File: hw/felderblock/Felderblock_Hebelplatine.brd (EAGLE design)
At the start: 50 x 78 mm, 35 parts, among them IC3 MCP23017SP, X1 I2C-1, X4 I2C-2

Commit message: tweaked layout
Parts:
- moved R25 2.84 mm to (7.62, 41.9)
- moved R27 2.54 mm to (7.62, 38.7)
- moved R16 1.91 mm to (27.9, 38.7)
- moved R20 1.90 mm to (27.9, 34.9)
- moved R28 1.27 mm to (27.9, 25.4)
- moved R22 0.64 mm to (27.9, 74.3)
- turned LED5 to 0 degrees
- turned LED6 to 0 degrees
- turned LED7 to 0 degrees
- turned LED8 to 0 degrees
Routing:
- net FST6_LED: track 34.7 -> 37.3 mm
- net FST8: track 35.6 -> 37.5 mm
- net FST4_LED: track 49.6 -> 51.3 mm
- net N$15: track 5.91 -> 4.60 mm
- net N$12: track 6.88 -> 8.09 mm
- net N$10: track 9.31 -> 10.5 mm
- net FST5: track 55.7 -> 54.6 mm
- net FST7_LED: track 58.2 -> 57.1 mm
- net FST7: track 20.9 -> 21.5 mm
- net FST3_LED: track 29.2 -> 28.6 mm

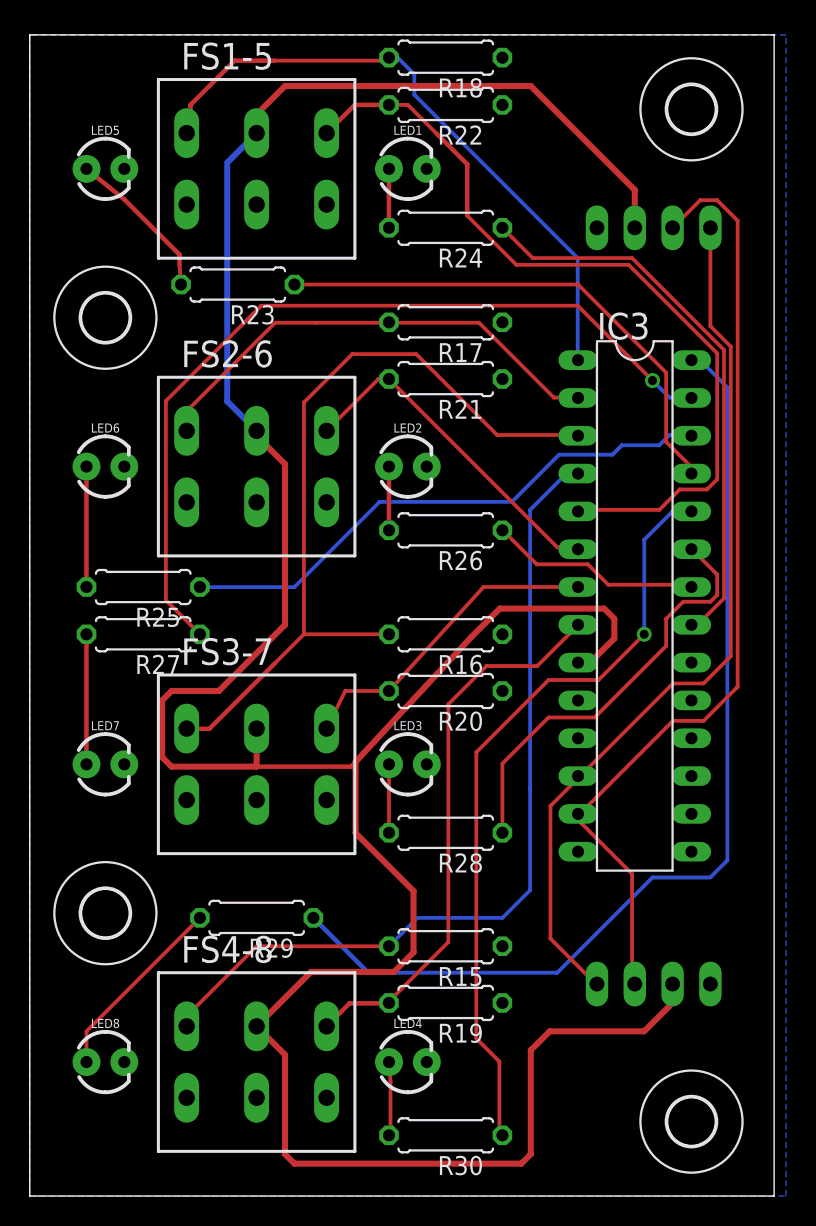
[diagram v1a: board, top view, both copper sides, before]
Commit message: moved I2C connectors
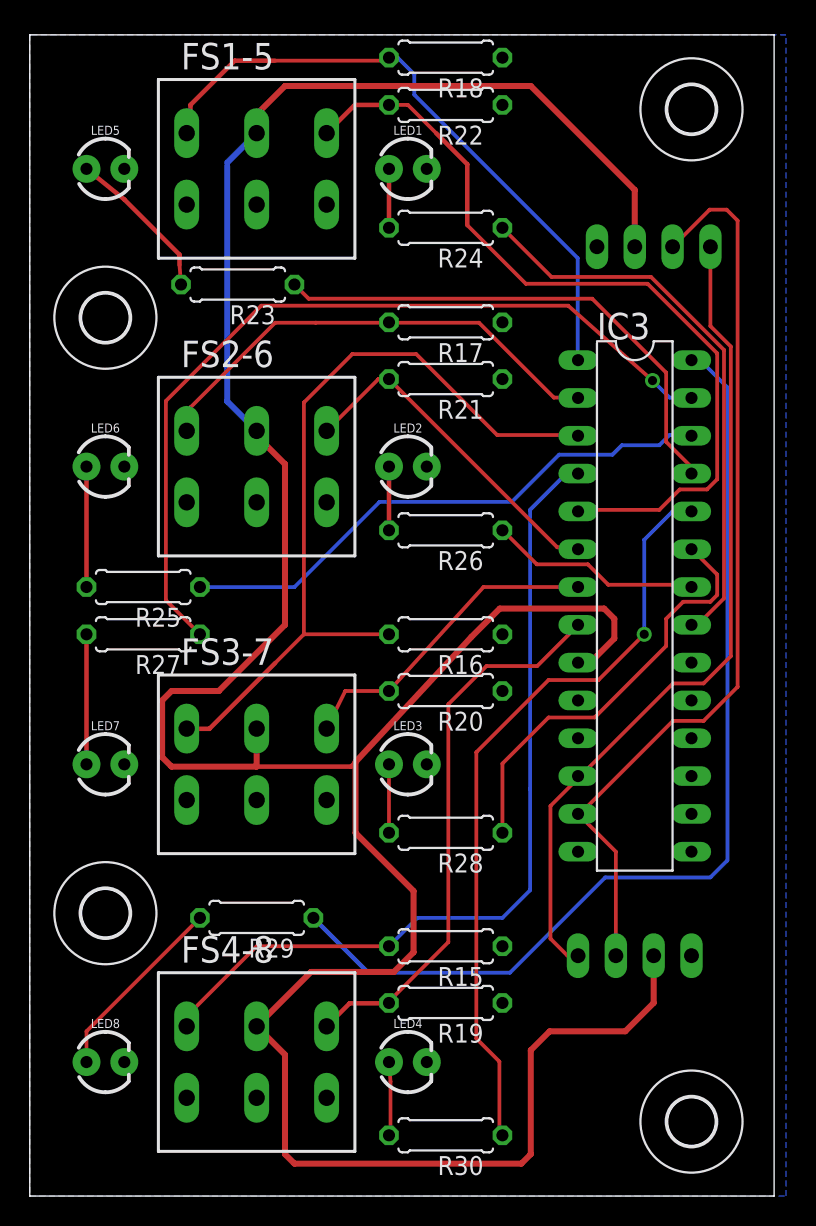
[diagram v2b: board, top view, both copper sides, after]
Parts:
- moved X4 2.29 mm to (40.6, 17.1)
- moved X1 1.27 mm to (41.9, 64.8)
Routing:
- net SCL: track 59.0 -> 55.7 mm
- net SDA: track 64.3 -> 61.8 mm
- net +5V: track 197.5 -> 199.4 mm

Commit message: changed I2C connectors
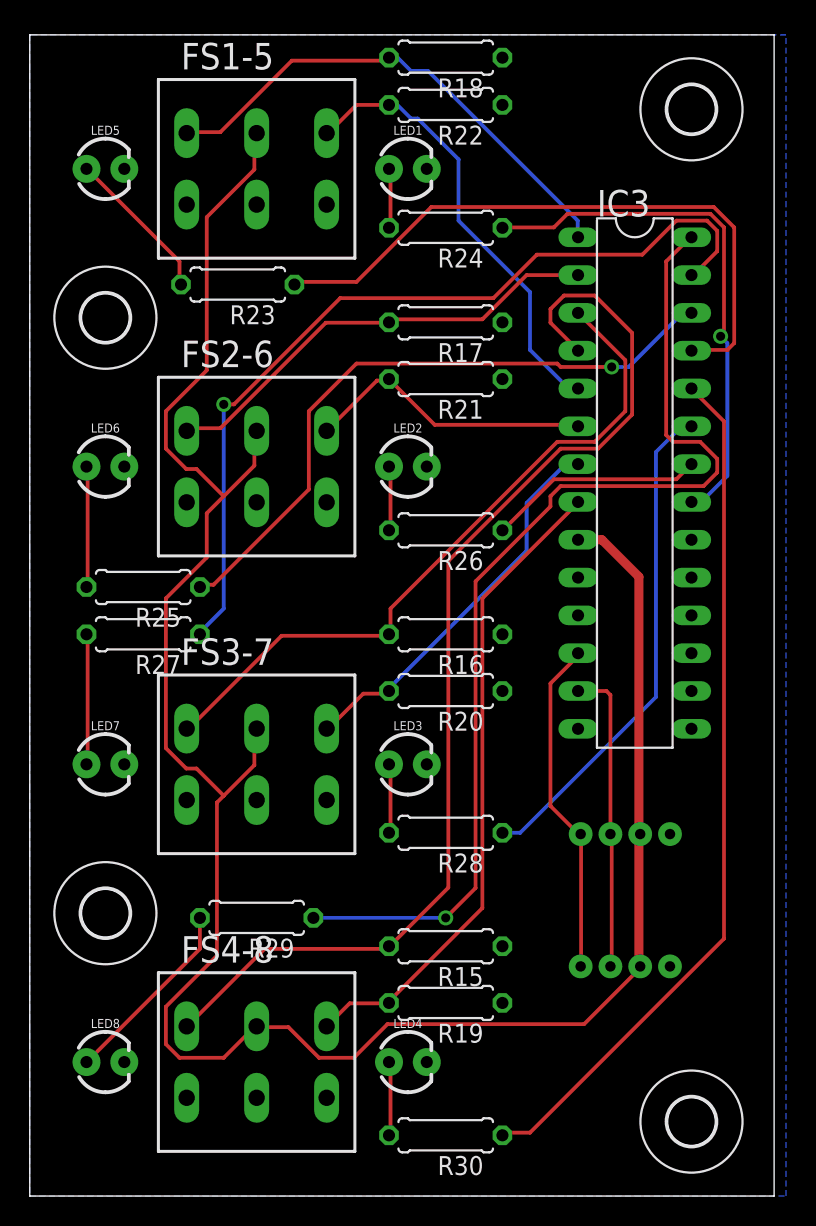
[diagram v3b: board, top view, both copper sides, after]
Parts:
- removed X1: I2C-1, con-molex:22-23-2041
- removed X4: I2C-2, con-molex:22-23-2041
- added I2C-1, I2C-2: (no value), SparkFun-Connectors:JST-4-PTH-VERT
- moved IC3 8.26 mm to (40.6, 48.9)
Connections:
- net +5V: now also I2C-1.3, I2C-2.3; no longer X1.2, X4.2
- net GND: now also I2C-1.4, I2C-2.4; no longer X1.1, X4.1
- net SCL: now also I2C-1.1, I2C-2.1; no longer X1.4, X4.4
- net SDA: now also I2C-1.2, I2C-2.2; no longer X1.3, X4.3
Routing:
- net +5V: track 199.4 -> 149.7 mm
- net SDA: track 61.8 -> 20.6 mm
- net SCL: track 55.7 -> 22.7 mm
- net FST5: track 55.0 -> 30.3 mm
- net FST4: track 57.1 -> 75.7 mm
- net FST1: track 42.6 -> 34.0 mm
- net FST5_LED: track 34.9 -> 43.2 mm
- net FST4_LED: track 51.3 -> 58.3 mm, vias 1 -> 0
- net FST6_LED: track 37.3 -> 44.0 mm, vias 0 -> 1
- net FST3: track 53.8 -> 47.1 mm
- net FST8: track 37.5 -> 43.7 mm
- net FST3_LED: track 28.6 -> 33.7 mm
- net FST7: track 21.5 -> 26.4 mm
- net FST8_LED: track 67.4 -> 71.0 mm, vias 0 -> 1
- net FST6: track 23.1 -> 19.7 mm
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
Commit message: changed holes for switches to oval ones
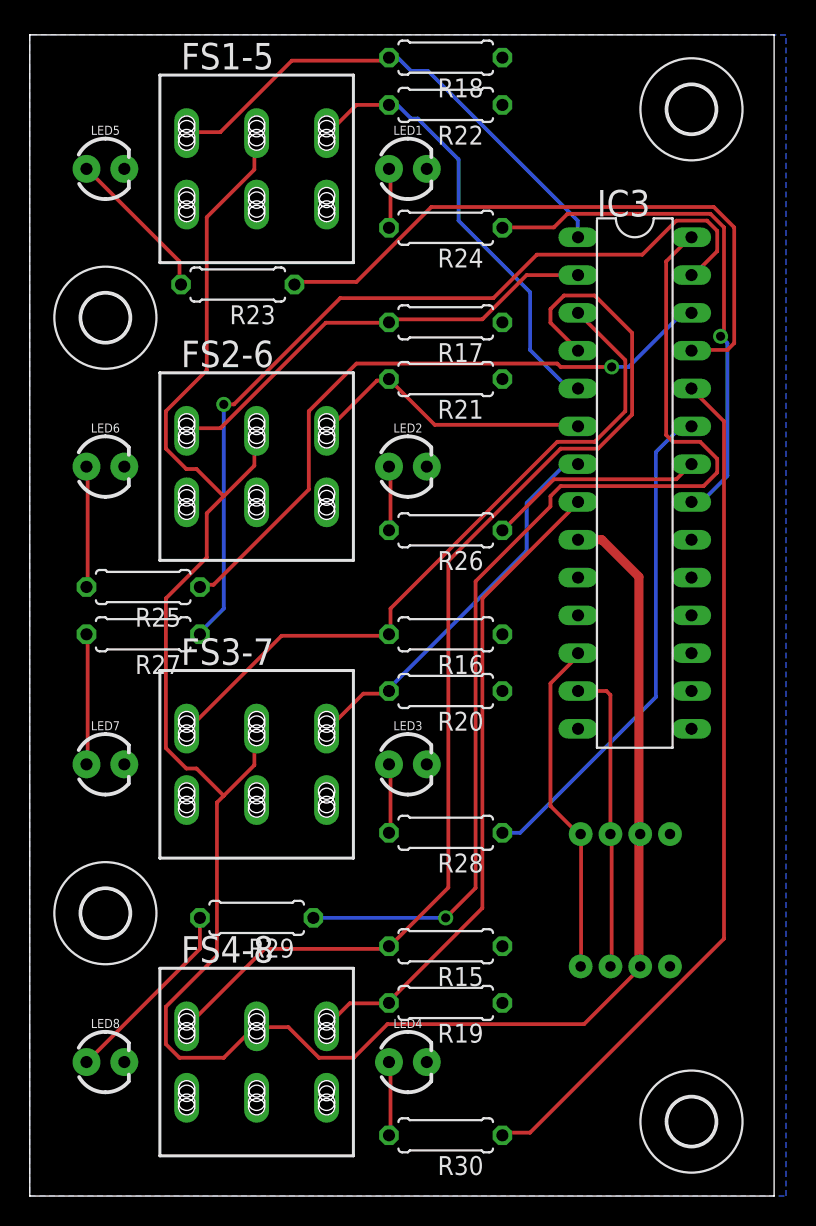
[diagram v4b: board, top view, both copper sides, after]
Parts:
- FS1-5, FS2-6, FS3-7, FS4-8: device Jens:DIL6_RUND -> Jens:DIL6_LANGLOCH
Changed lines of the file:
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@@
 <element name="R29" library="resistor" package="0207/7" value="1k" x="15.24" y="19.685" rot="R180"/>
 <element name="R30" library="resistor" package="0207/7" value="1k" x="27.94" y="5.08" rot="R180"/>
-<element name="FS1-5" library="Jens" package="DIL6_RUND" value="" x="15.24" y="70"/>
-<element name="FS2-6" library="Jens" package="DIL6_RUND" value="" x="15.24" y="50"/>
-<element name="FS3-7" library="Jens" package="DIL6_RUND" value="" x="15.24" y="30"/>
-<element name="FS4-8" library="Jens" package="DIL6_RUND" value="" x="15.24" y="10"/>
+<element name="FS1-5" library="Jens" package="DIL6_LANGLOCH" value="" x="15.24" y="70"/>
+<element name="FS2-6" library="Jens" package="DIL6_LANGLOCH" value="" x="15.24" y="50"/>
+<element name="FS3-7" library="Jens" package="DIL6_LANGLOCH" value="" x="15.24" y="30"/>
+<element name="FS4-8" library="Jens" package="DIL6_LANGLOCH" value="" x="15.24" y="10"/>
 <element name="H1" library="holes" package="3,2" value="MOUNT-HOLE3.2" x="44.45" y="74"/>
 <element name="H2" library="holes" package="3,2" value="MOUNT-HOLE3.2" x="44.45" y="6"/>

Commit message: some tuning
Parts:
- FS1-5, FS2-6, FS3-7, FS4-8: device Jens:DIL6_LANGLOCH -> Jens:DIL6_LARGE
- moved R18 0.64 mm to (27.9, 76.8)
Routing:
- net +5V: track 149.7 -> 182.0 mm
- net FST3: track 47.1 -> 53.6 mm
- net FST7_LED: track 58.4 -> 53.0 mm, vias 1 -> 2
- net FST6_LED: track 44.0 -> 48.4 mm
- net FST2: track 30.7 -> 33.2 mm
- net FST6: track 19.7 -> 21.3 mm
- net FST1: track 34.0 -> 35.7 mm
- net FST7: track 26.4 -> 26.9 mm
